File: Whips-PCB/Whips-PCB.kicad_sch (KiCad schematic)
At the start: 5 parts, among them SW1 SW_DIP_x05, U1 Teensy4.0, U2 MAX485E, U3 SN74AHCT125, U4 TSR_1-2450

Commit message: improved rs422
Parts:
- removed SW1: SW_DIP_x05, symbol Switch:SW_DIP_x05
- added C1: 0.1uF, symbol Device:C
- added C2: 10uF, symbol Device:C
- added R1, R2: 20K, symbol Device:R_US
- added R3, R4: 10K, symbol Device:R_US
- added R5: 120, symbol Device:R_US
- added SW2: SW_DIP_x06, symbol Switch:SW_DIP_x06
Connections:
- net +3.3V: now also C1.1, C2.1, R1.1, R3.1, R4.1
- net GND: now also C1.2, C2.2, R2.2, SW2.10, SW2.11, SW2.12, SW2.8, SW2.9
- net RX: now also R4.2
- net at U1.4 (2_OUT2): now also SW2.5
- net at U1.5 (3_LRCLK2): now also SW2.4
- net at U1.6 (4_BCLK2): now also SW2.3
- net at U1.7 (5_IN2): now also SW2.2
- net at U1.8 (6_OUT1D): now also SW2.1
- net at U2.4 (DI): now also R3.2
- net A: now reaches U2.6 (A)
- net A: now also R1.2, SW2.7
- net B: now reaches U2.7 (B)
- net B: now also R2.1, R5.2
- new net: R5.1, SW2.6
- no-connect marks 7 -> 6
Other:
- note added: "SERIAL RS422 DRIVER"
- note added: "SET DIP SWITCH #6 TO CONNECT 120 OHM TERMINATING RESISTOR AT THE FARTHEST WHIP"
- note removed: "SERIAL IN"
- moved on the sheet: U1, U2, U3

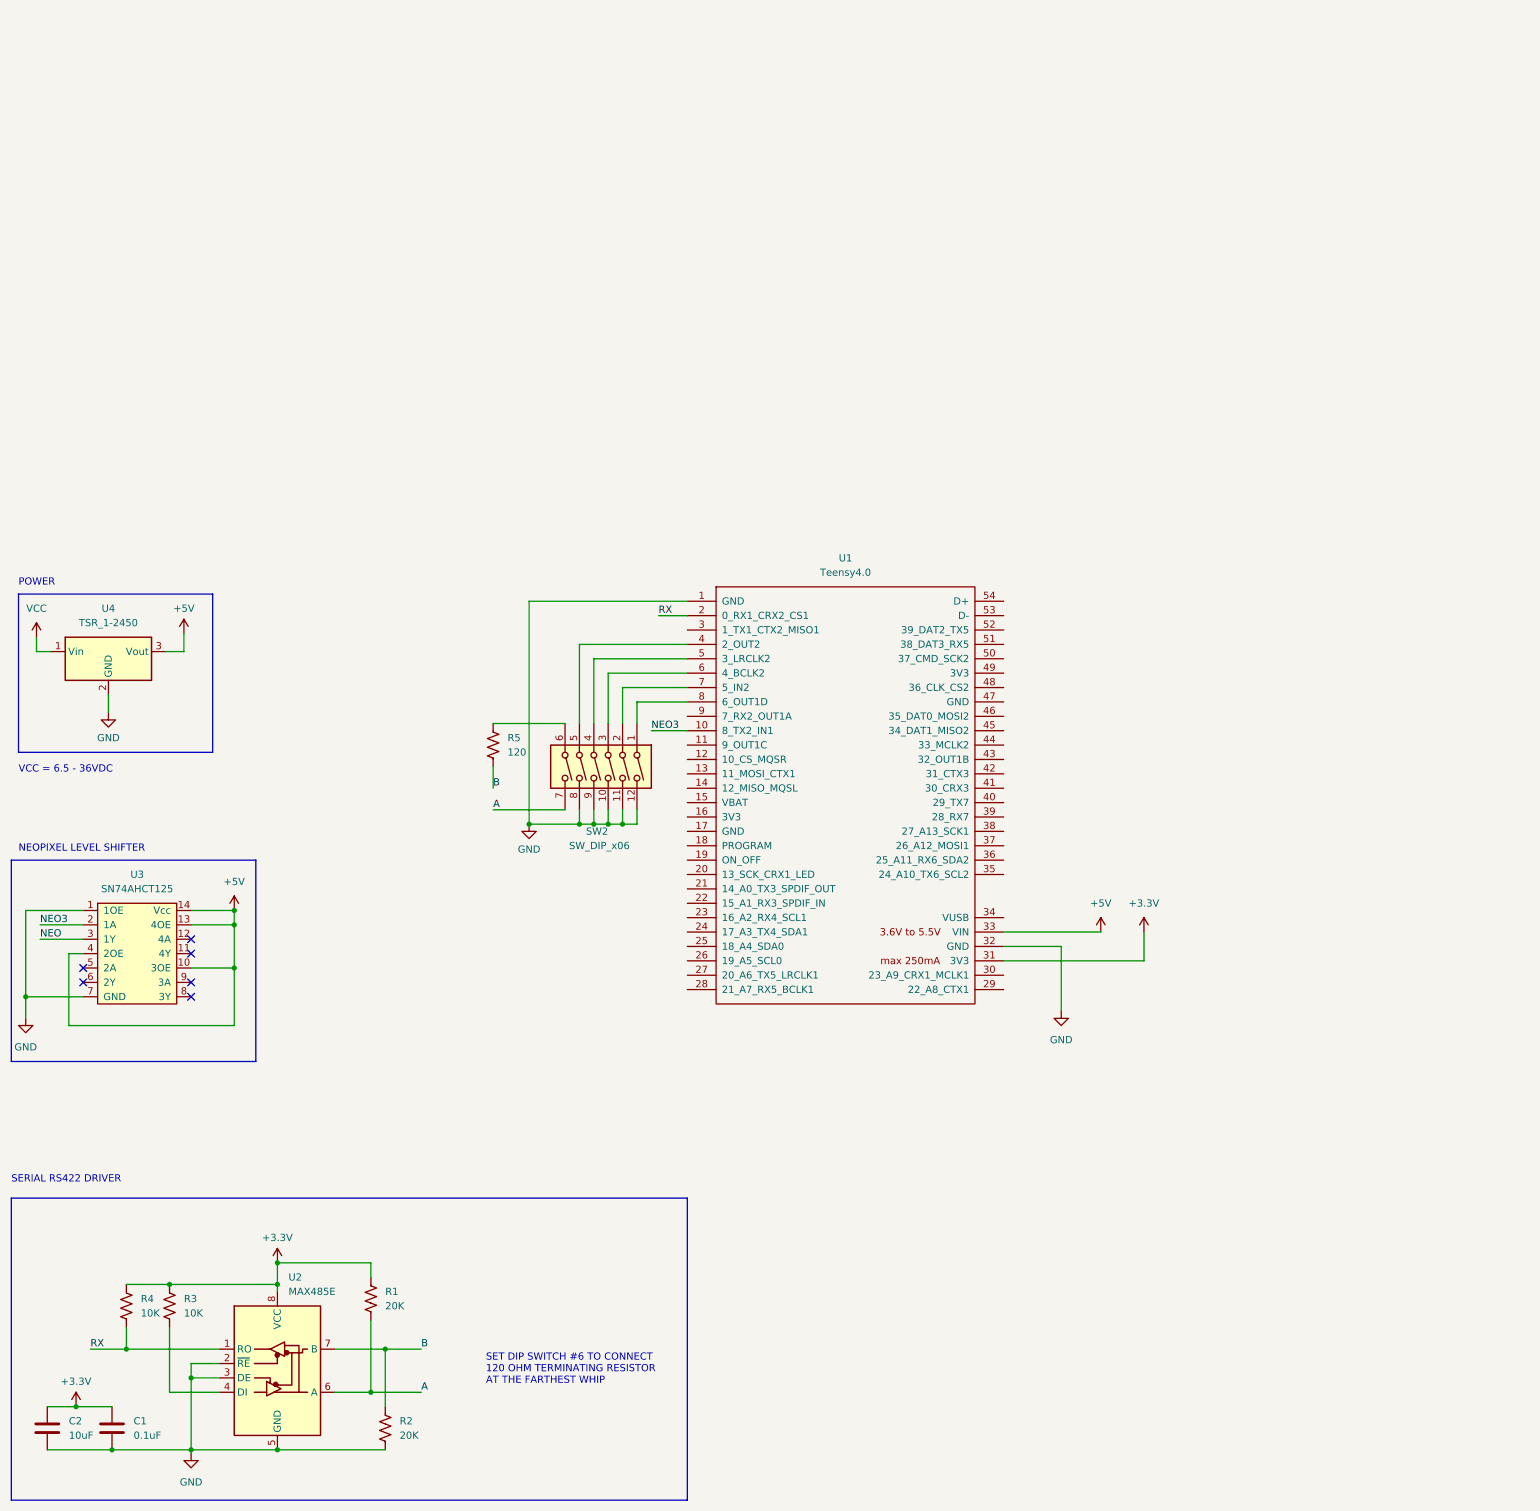
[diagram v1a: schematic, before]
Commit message: updated schematic to reflect audio and sd card
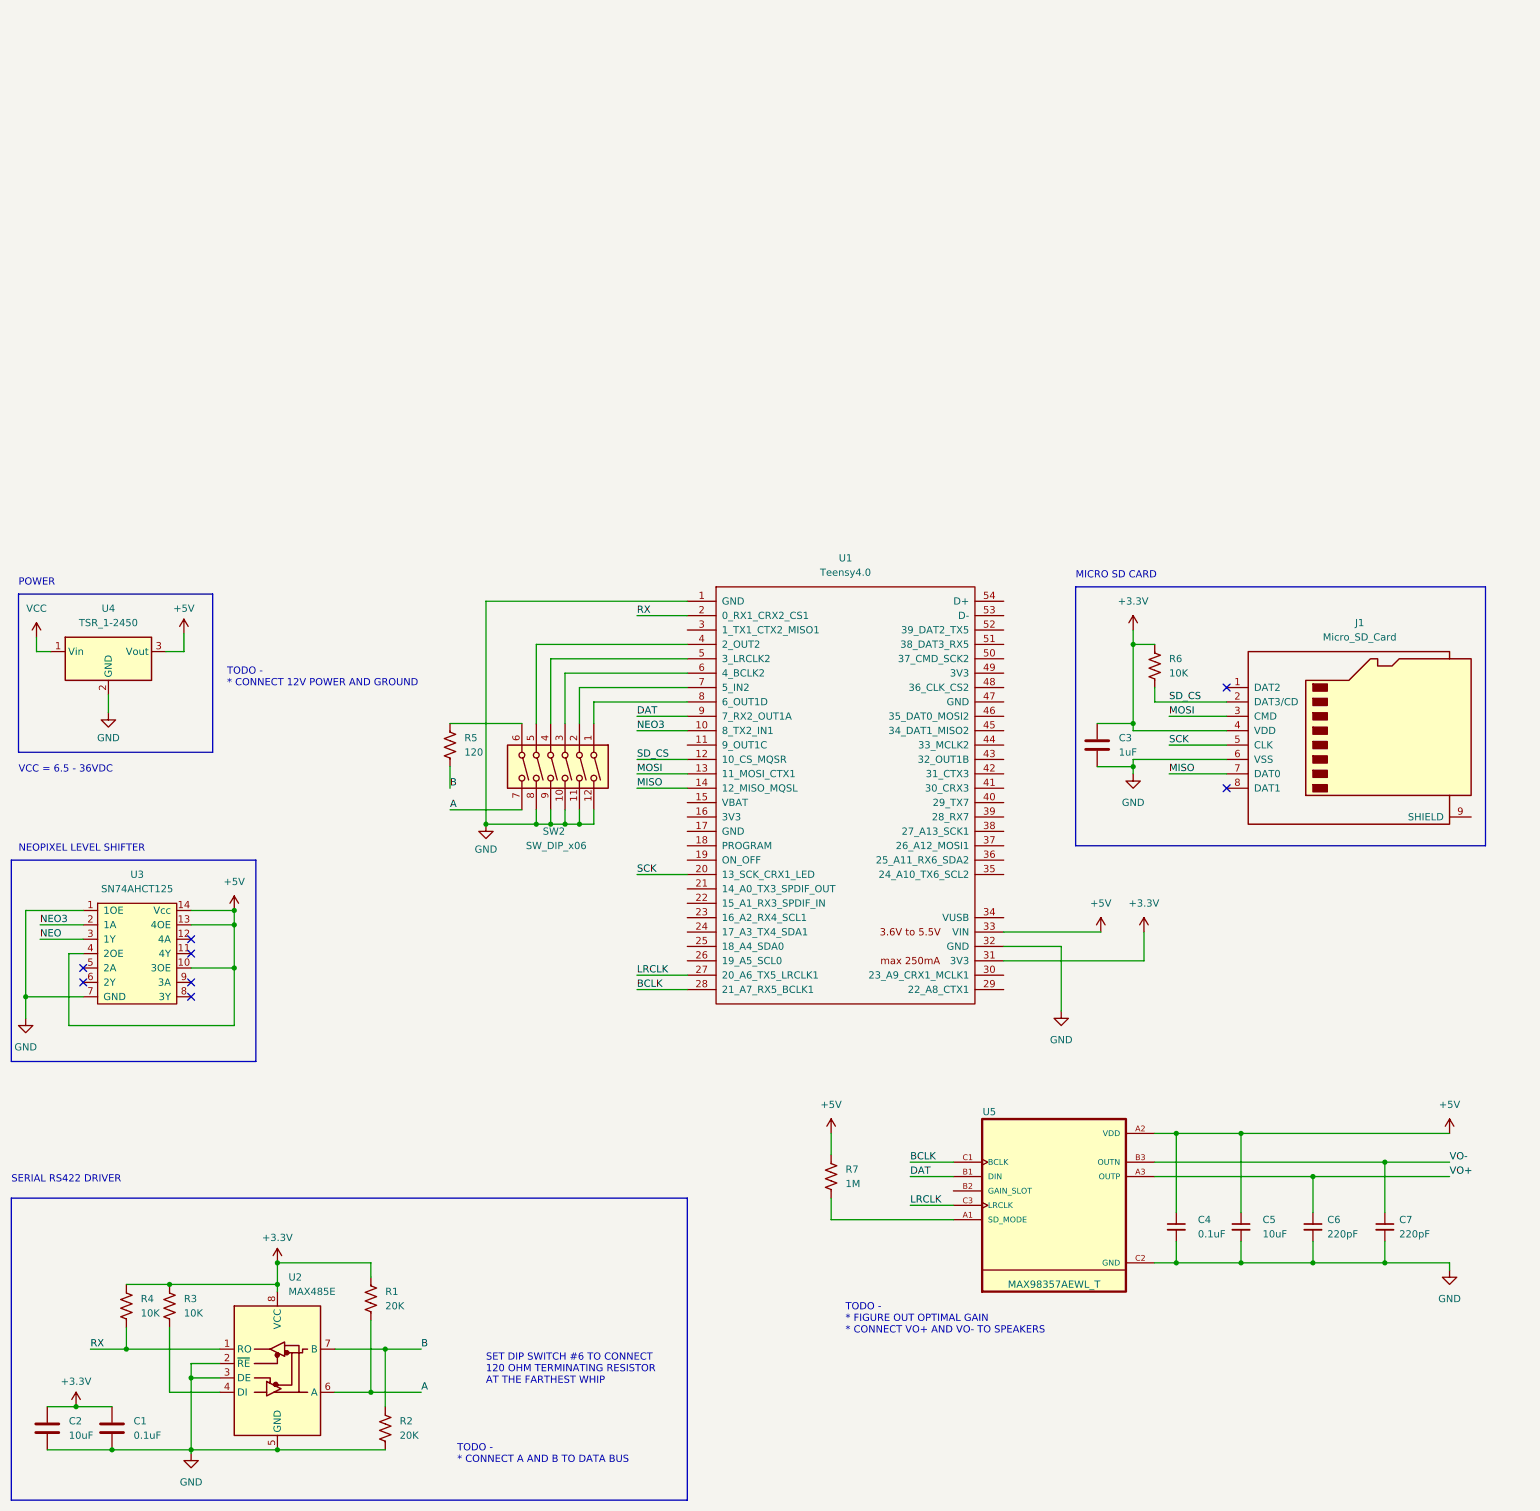
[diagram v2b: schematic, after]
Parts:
- added C3: 1uF, symbol Device:C
- added C4: 0.1uF, symbol Device:C_Small
- added C5: 10uF, symbol Device:C_Small
- added C6, C7: 220pF, symbol Device:C_Small
- added J1: Micro_SD_Card, symbol Connector:Micro_SD_Card
- added R6: 10K, symbol Device:R_US
- added R7: 1M, symbol Device:R_US
- added U5: MAX98357AEWL_T, MAX98357AEWL_T:BGA9N40P3X3_134X143X69N, symbol Joels KiCad Symbol Library:MAX98357AEWL_T
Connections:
- net +3.3V: now also C3.1, J1.4 (VDD), R6.1
- net +5V: now also C4.1, C5.1, R7.1, U5.A2 (VDD)
- net GND: now also C3.2, C4.2, C5.2, C6.2, C7.2, J1.6 (VSS), U5.C2 (GND)
- net SD_CS: now reaches U1.12 (10_CS_MQSR)
- net SD_CS: now also J1.2 (DAT3/CD), R6.2
- net MOSI: now reaches U1.13 (11_MOSI_CTX1)
- net MOSI: now also J1.3 (CMD)
- net MISO: now reaches U1.14 (12_MISO_MQSL)
- net MISO: now also J1.7 (DAT0)
- net SCK: now reaches U1.20 (13_SCK_CRX1_LED)
- net SCK: now also J1.5 (CLK)
- net LRCLK: now reaches U1.27 (20_A6_TX5_LRCLK1)
- net LRCLK: now also U5.C3 (LRCLK)
- net BCLK: now reaches U1.28 (21_A7_RX5_BCLK1)
- net BCLK: now also U5.C1 (BCLK)
- net DAT: now reaches U1.9 (7_RX2_OUT1A)
- net DAT: now also U5.B1 (DIN)
- new net: R7.2, U5.A1 (SD_MODE)
- new net VO+: C6.1, U5.A3 (OUTP)
- new net VO-: C7.1, U5.B3 (OUTN)
- no-connect marks 6 -> 8
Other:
- note added: "MICRO SD CARD"
- note added: "TODO - * CONNECT 12V POWER AND GROUND"
- note added: "TODO - * CONNECT A AND B TO DATA BUS"
- note added: "TODO - * FIGURE OUT OPTIMAL GAIN * CONNECT VO+ AND VO- TO SPEAKERS"
- moved on the sheet: R5, SW2

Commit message: volume adjustment. Use maximum gain in hardware
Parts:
- added R8: 100K, symbol Device:R_US
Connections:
- net GND: now also R8.2
- net at U5.B2 (GAIN_SLOT): now also R8.1
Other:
- note added: "TODO - * CONNECT VO+ AND VO- TO SPEAKERS"
- note removed: "TODO - * FIGURE OUT OPTIMAL GAIN * CONNECT VO+ AND VO- TO SPEAKERS"
- moved on the sheet: R7
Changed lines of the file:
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@@
+    (stroke (width 0) (type default))
+  )
+  (wire (pts (xy 172.72 130.81) (xy 182.88 130.81))
     (stroke (width 0) (type default))
   )
@@
     (stroke (width 0) (type default))
   )
+  (wire (pts (xy 172.72 124.46) (xy 172.72 130.81))
+    (stroke (width 0) (type default))
+  )
   (wire (pts (xy 19.05 81.28) (xy 19.05 96.52))
     (stroke (width 0) (type default))
@@
     (stroke (width 0) (type default))
   )
+  (wire (pts (xy 162.56 124.46) (xy 172.72 124.46))
+    (stroke (width 0) (type default))
+  )
   (wire (pts (xy 33.655 43.18) (xy 33.655 46.355))
     (stroke (width 0) (type default))
@@
     (stroke (width 0) (type default))
   )
+  (wire (pts (xy 162.56 132.08) (xy 162.56 140.97))
+    (stroke (width 0) (type default))
+  )
   (wire (pts (xy 220.98 57.15) (xy 231.14 57.15))
     (stroke (width 0) (type default))
@@
     (stroke (width 0) (type default))
   )
-  (wire (pts (xy 161.29 120.65) (xy 161.29 124.46))
+  (wire (pts (xy 153.67 120.65) (xy 153.67 124.46))
     (stroke (width 0) (type default))
   )
@@
     (stroke (width 0) (type default))
   )
-  (wire (pts (xy 161.29 135.89) (xy 161.29 132.08))
+  (wire (pts (xy 153.67 135.89) (xy 153.67 132.08))
     (stroke (width 0) (type default))
   )
@@
     (stroke (width 0) (type default))
   )
-  (wire (pts (xy 182.88 135.89) (xy 161.29 135.89))
+  (wire (pts (xy 182.88 135.89) (xy 153.67 135.89))
     (stroke (width 0) (type default))
   )
@@
     (fill (type none))
   )
-  (text "TODO - \n* FIGURE OUT OPTIMAL GAIN\n* CONNECT VO+ AND VO- TO SPEAKERS"
-    (at 163.83 156.21 0)
+  (text "TODO - \n* CONNECT VO+ AND VO- TO SPEAKERS" (at 163.83 156.21 0)
     (effects (font (size 1.27 1.27)) (justify left bottom))
   )
@@
     )
   )
-  (symbol (lib_id "power:+5V") (at 161.29 120.65 0) (unit 1)
-    (in_bom yes) (on_board yes) (dnp no) (fields_autoplaced)
-    (property "Reference" "#PWR015" (at 161.29 124.46 0)
-      (effects (font (size 1.27 1.27)) hide)
-    )
-    (property "Value" "+5V" (at 161.29 115.57 0)
-      (effects (font (size 1.27 1.27)))
-    )
-    (property "Footprint" "" (at 161.29 120.65 0)
-      (effects (font (size 1.27 1.27)) hide)
-    )
-    (property "Datasheet" "" (at 161.29 120.65 0)
+  (symbol (lib_id "power:+5V") (at 153.67 120.65 0) (unit 1)
+    (in_bom yes) (on_board yes) (dnp no) (fields_autoplaced)
+    (property "Reference" "#PWR015" (at 153.67 124.46 0)
+      (effects (font (size 1.27 1.27)) hide)
+    )
+    (property "Value" "+5V" (at 153.67 115.57 0)
+      (effects (font (size 1.27 1.27)))
+    )
+    (property "Footprint" "" (at 153.67 120.65 0)
+      (effects (font (size 1.27 1.27)) hide)
+    )
+    (property "Datasheet" "" (at 153.67 120.65 0)
       (effects (font (size 1.27 1.27)) hide)
     )
@@
     )
   )
+  (symbol (lib_id "Device:R_US") (at 162.56 128.27 0) (unit 1)
+    (in_bom yes) (on_board yes) (dnp no) (fields_autoplaced)
+    (property "Reference" "R8" (at 165.1 127 0)
+      (effects (font (size 1.27 1.27)) (justify left))
+    )
+    (property "Value" "100K" (at 165.1 129.54 0)
+      (effects (font (size 1.27 1.27)) (justify left))
+    )
+    (property "Footprint" "" (at 163.576 128.524 90)
+      (effects (font (size 1.27 1.27)) hide)
+    )
+    (property "Datasheet" "~" (at 162.56 128.27 0)
+      (effects (font (size 1.27 1.27)) hide)
+    )
+    (pin "1")
+    (pin "2")
+    (instances
+      (project "Whips-PCB"
+        (path "/f51f4695-2f3c-4442-ab83-4885bbbb2720"
+          (reference "R8") (unit 1)
+        )
+      )
+    )
+  )
   (symbol (lib_id "power:+5V") (at 270.51 120.65 0) (unit 1)
     (in_bom yes) (on_board yes) (dnp no) (fields_autoplaced)
@@
     )
   )
-  (symbol (lib_id "Device:R_US") (at 161.29 128.27 0) (unit 1)
-    (in_bom yes) (on_board yes) (dnp no) (fields_autoplaced)
-    (property "Reference" "R7" (at 163.83 127 0)
-      (effects (font (size 1.27 1.27)) (justify left))
-    )
-    (property "Value" "1M" (at 163.83 129.54 0)
-      (effects (font (size 1.27 1.27)) (justify left))
-    )
-    (property "Footprint" "" (at 162.306 128.524 90)
-      (effects (font (size 1.27 1.27)) hide)
-    )
-    (property "Datasheet" "~" (at 161.29 128.27 0)
+  (symbol (lib_id "Device:R_US") (at 153.67 128.27 0) (unit 1)
+    (in_bom yes) (on_board yes) (dnp no) (fields_autoplaced)
+    (property "Reference" "R7" (at 156.21 127 0)
+      (effects (font (size 1.27 1.27)) (justify left))
+    )
+    (property "Value" "1M" (at 156.21 129.54 0)
+      (effects (font (size 1.27 1.27)) (justify left))
+    )
+    (property "Footprint" "" (at 154.686 128.524 90)
+      (effects (font (size 1.27 1.27)) hide)
+    )
+    (property "Datasheet" "~" (at 153.67 128.27 0)
       (effects (font (size 1.27 1.27)) hide)
     )
@@
         )
       )
+    )
+  )
+  (symbol (lib_id "power:GND") (at 162.56 140.97 0) (unit 1)
+    (in_bom yes) (on_board yes) (dnp no) (fields_autoplaced)
+    (property "Reference" "#PWR018" (at 162.56 147.32 0)
+      (effects (font (size 1.27 1.27)) hide)
+    )
+    (property "Value" "GND" (at 162.56 146.05 0)
+      (effects (font (size 1.27 1.27)))
+    )
+    (property "Footprint" "" (at 162.56 140.97 0)
+      (effects (font (size 1.27 1.27)) hide)
+    )
+    (property "Datasheet" "" (at 162.56 140.97 0)
+      (effects (font (size 1.27 1.27)) hide)
+    )
+    (pin "1")
+    (instances
+      (project "Whips-PCB"
+        (path "/f51f4695-2f3c-4442-ab83-4885bbbb2720"
+          (reference "#PWR018") (unit 1)
+        )
+      )
